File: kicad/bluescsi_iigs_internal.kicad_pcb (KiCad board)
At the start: 2 copper layers, 56.6 x 53.3 mm, 24 parts, among them J1 Conn_02x13_Odd_Even, J2 Conn_02x13_Odd_Even, J3 105162-0001, J4 Conn_01x02_Male, SW1 SW_SPDT, U1 YAAJ_BluePill, U2 UC560x, UCC56xx, U3 UC560x, UCC56xx, U4 AMS1117-5.0

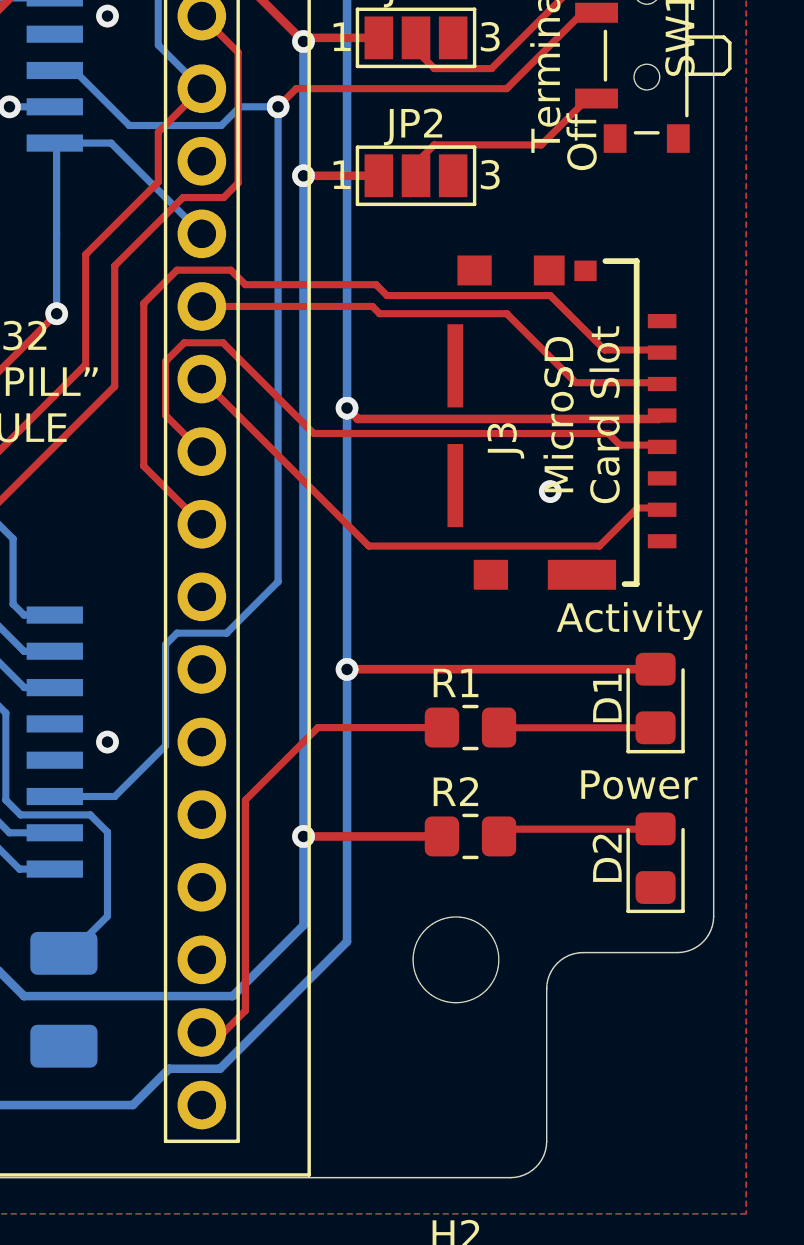
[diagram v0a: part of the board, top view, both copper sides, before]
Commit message: Add p-mosfet driver for activity LED
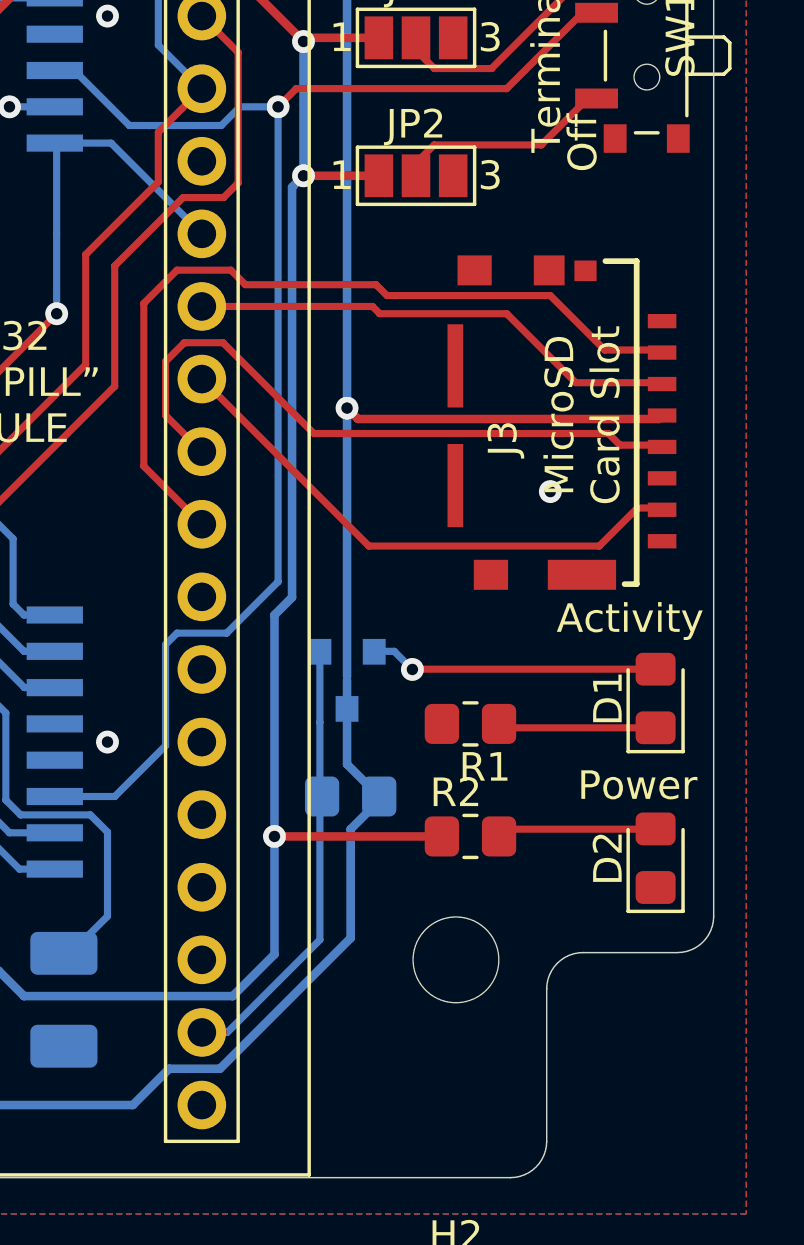
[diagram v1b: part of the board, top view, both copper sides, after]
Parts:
- added Q1: Q_PMOS_GSD, Package_TO_SOT_SMD:SOT-23, B.Cu at (172.7, 84.2)
- added R3: 10K, Resistor_SMD:R_0805_2012Metric_Pad1.20x1.40mm_HandSolder, B.Cu at (172.8, 88.3)
- R1: value 330 -> 470
- R2: value 470 -> 1K
- moved R1 0.13 mm to (177.0, 85.7), turned to 0 degrees
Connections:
- D1 pad 2: +3V3 -> Net-(D1-Pad2)
- R1 pad 1: Net-(D1-Pad1) -> GND
- R1 pad 2: /DISK_ACT -> Net-(D1-Pad1)
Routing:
- net Net-(D1-Pad2): track 0.00 -> 10.1 mm, vias 0 -> 1
- net +3V3: track 85.5 -> 75.7 mm, vias 3 -> 2
- net +5V: track 97.4 -> 98.5 mm
- net /DISK_ACT: track 17.1 -> 16.3 mm

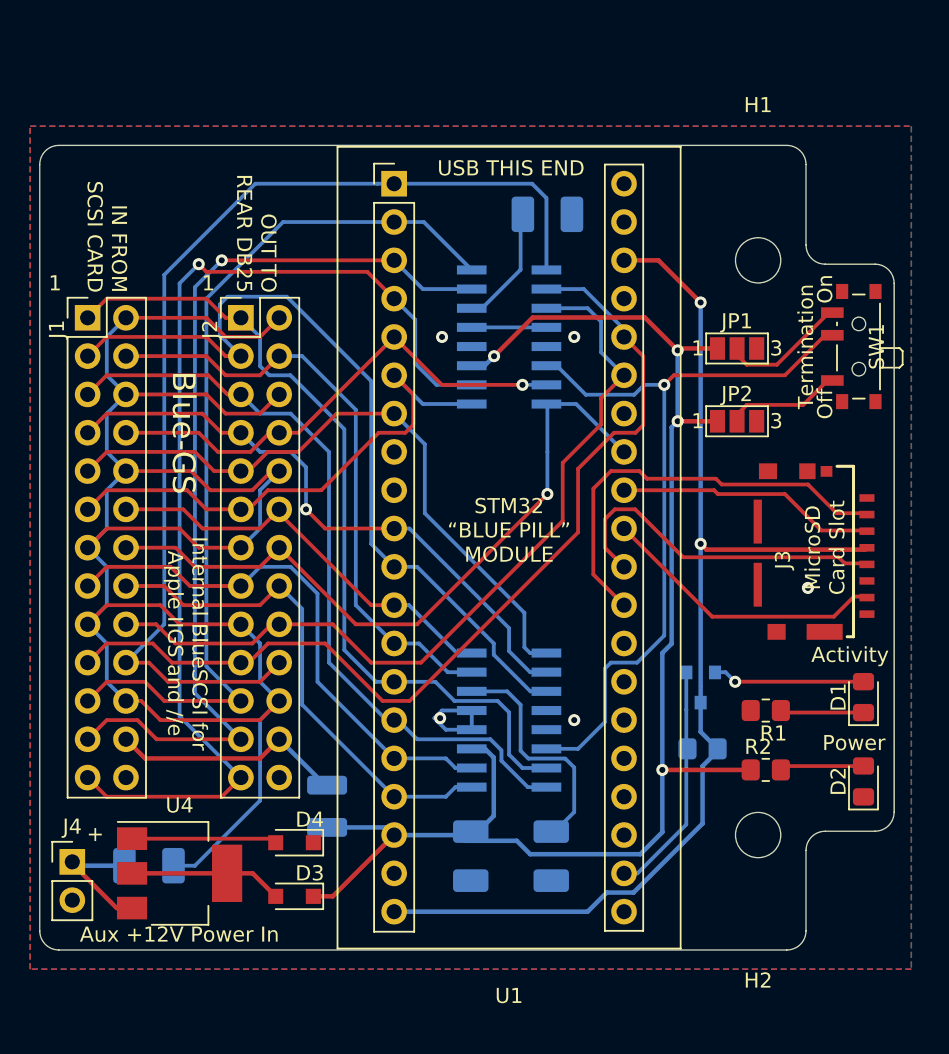
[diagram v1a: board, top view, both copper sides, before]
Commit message: Added connector for external activity LED
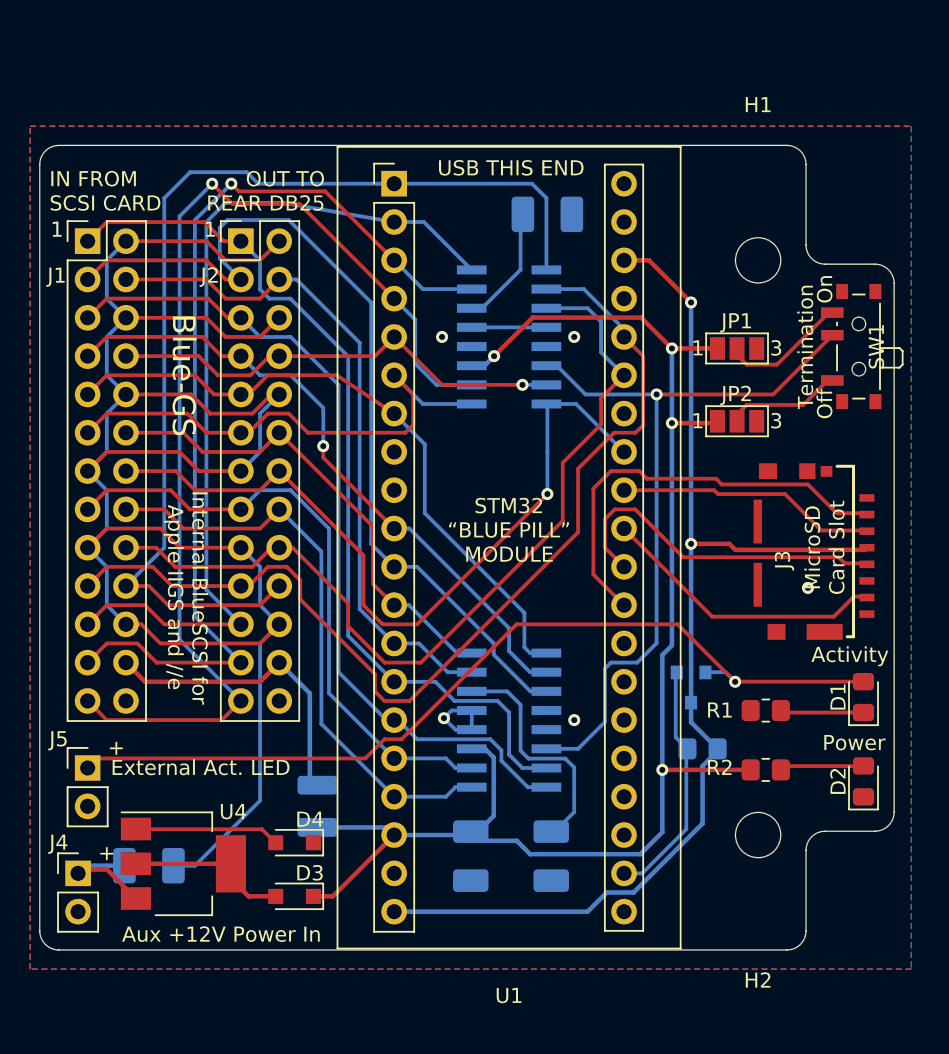
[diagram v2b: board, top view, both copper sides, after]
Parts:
- added J5: Conn_01x02_Male, Connector_PinHeader_2.54mm:PinHeader_1x02_P2.54mm_Vertical, F.Cu at (132.1, 89.5)
- moved J1 5.08 mm to (132.1, 54.6)
- moved J2 5.08 mm to (142.2, 54.6)
- moved J4 0.85 mm to (131.4, 96.5)
- moved U4 0.68 mm to (138.4, 95.9)
- moved F1 0.64 mm to (147.3, 92.1)
- moved Q1 0.63 mm to (172.1, 84.2)
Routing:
- net Net-(D1-Pad2): track 10.1 -> 59.1 mm
- net /SCSI_TERMPWR: track 15.6 -> 21.0 mm
- net /SCSI_MSG: track 54.7 -> 59.8 mm
- net /SCSI_DB1: track 34.2 -> 39.3 mm
- net /SCSI_I_O: track 50.8 -> 55.9 mm
- net /SCSI_DB0: track 36.5 -> 41.6 mm
- net /SCSI_C_D: track 40.2 -> 45.1 mm
- net /SCSI_SEL: track 28.8 -> 33.2 mm
- net /SCSI_REQ: track 55.2 -> 59.6 mm
- net /SCSI_DBP: track 47.1 -> 51.2 mm
- net GND: track 136.7 -> 140.5 mm
- net /SCSI_DB3: track 63.2 -> 66.7 mm
- net /SCSI_DB2: track 54.5 -> 57.5 mm
- net /SCSI_RST: track 40.6 -> 43.0 mm
- net /SCSI_ATN: track 33.4 -> 31.3 mm
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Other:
- board text added: "External Act. LED"
- board text added: "WARNING: USB should not be used while powered from SCSI TermPwr or Aux +12V"
- board text removed: "WARNING: USB should not be used while powered from SCSI Termination Power or Aux +12V Power"

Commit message: Replace mounting holes with Keystone 7774 brackets
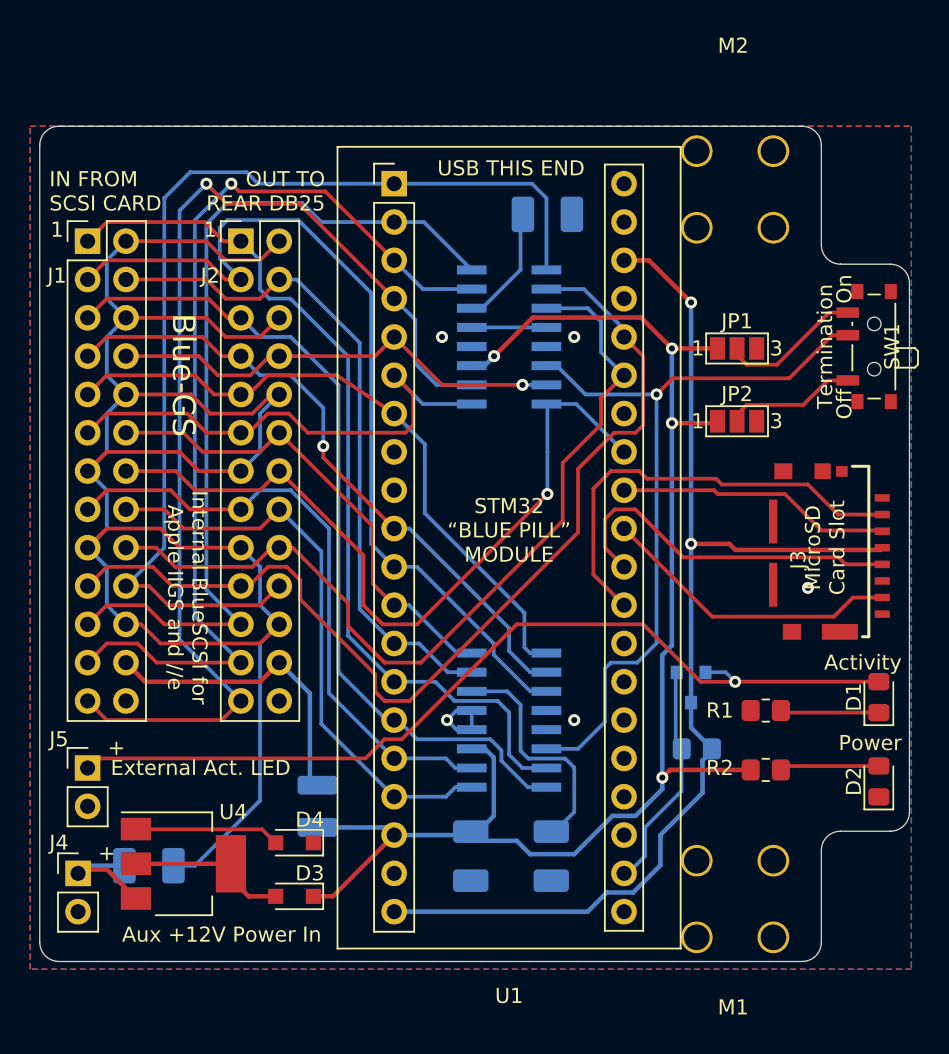
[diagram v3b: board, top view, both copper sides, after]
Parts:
- removed H1, H2: MountingHole, MountingHole:MountingHole_3mm
- added M1: Screw_Terminal_01x01, my library:keystone-7774, F.Cu at (180.7, 100.8)
- added M2: Screw_Terminal_01x01, my library:keystone-7774, F.Cu at (180.7, 53.7)
- moved D1 1.02 mm to (184.5, 84.8)
- moved D2 1.02 mm to (184.5, 90.4)
- moved J3 1.02 mm to (177.4, 75.2)
- moved SW1 1.02 mm to (183.9, 61.6)
- moved R3 0.38 mm to (172.5, 88.3)
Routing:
- net /DISK_ACT: track 16.7 -> 15.1 mm
- net +5V: track 98.8 -> 97.3 mm
- net /TERM_DISC: track 50.1 -> 51.4 mm
- net /TERM_DIS: track 7.57 -> 8.84 mm
- net /TERM_EN: track 8.57 -> 9.84 mm
- net /SD_CSK: track 22.8 -> 23.9 mm
- net /SD_CS: track 28.4 -> 29.4 mm
- net Net-(D1-Pad2): track 59.1 -> 60.1 mm
- net Net-(D1-Pad1): track 5.55 -> 6.56 mm
- net /SD_MOSI: track 17.2 -> 18.2 mm
- net /SD_MISO: track 19.1 -> 20.1 mm
- net +3V3: track 76.0 -> 76.7 mm
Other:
- board size 56.6 x 53.3 mm -> 57.7 x 55.4 mm

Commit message: Adjust screw hole in slightly to account for screw width add silkscreen on rear for card slot
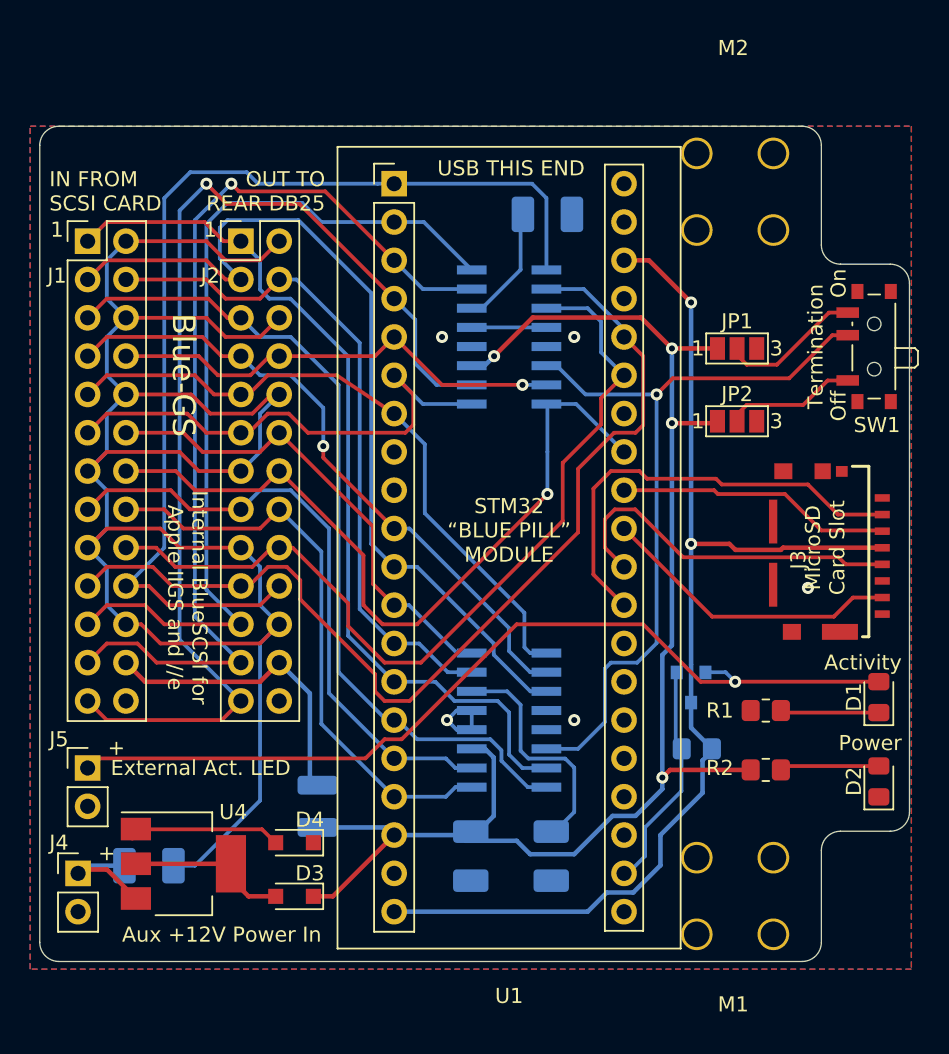
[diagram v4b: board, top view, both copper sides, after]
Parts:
- moved M1 0.20 mm to (180.7, 100.6)
- moved M2 0.15 mm to (180.7, 53.9)
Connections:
- M1 pad 1: (no net) -> GND
- M2 pad 1: (no net) -> GND
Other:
- board text added: "For Apple Rev. C SCSI and cards with compatible connector"
- board text added: "PWR"
- board text added: "WARNING: USB power should not be used while powered from SCSI or Aux +12V"
- board text added: "| CARD |"
- board text removed: "For Apple Rev. C SCSI card, and cards with compatible connector"
- board text removed: "POWER"
- board text removed: "WARNING: USB should not be used while powered from SCSI TermPwr or Aux +12V"

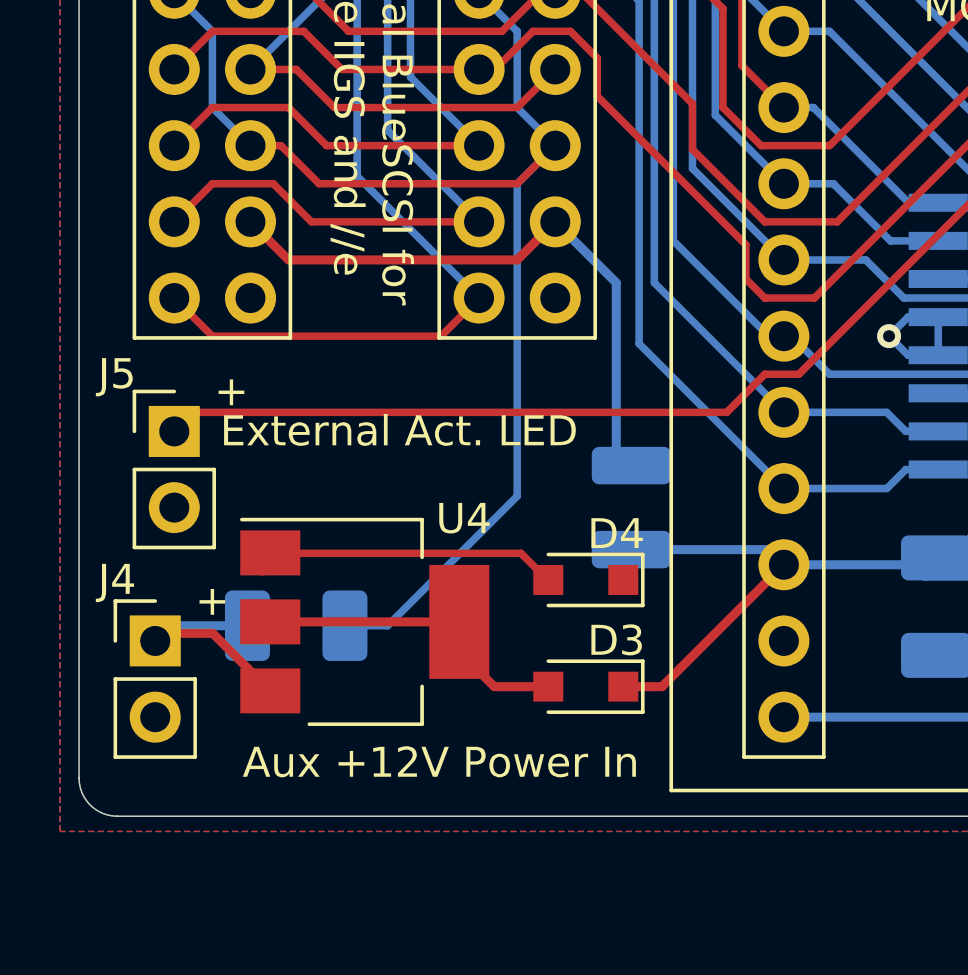
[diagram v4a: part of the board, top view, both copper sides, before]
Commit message: pth regulator hanging off the side
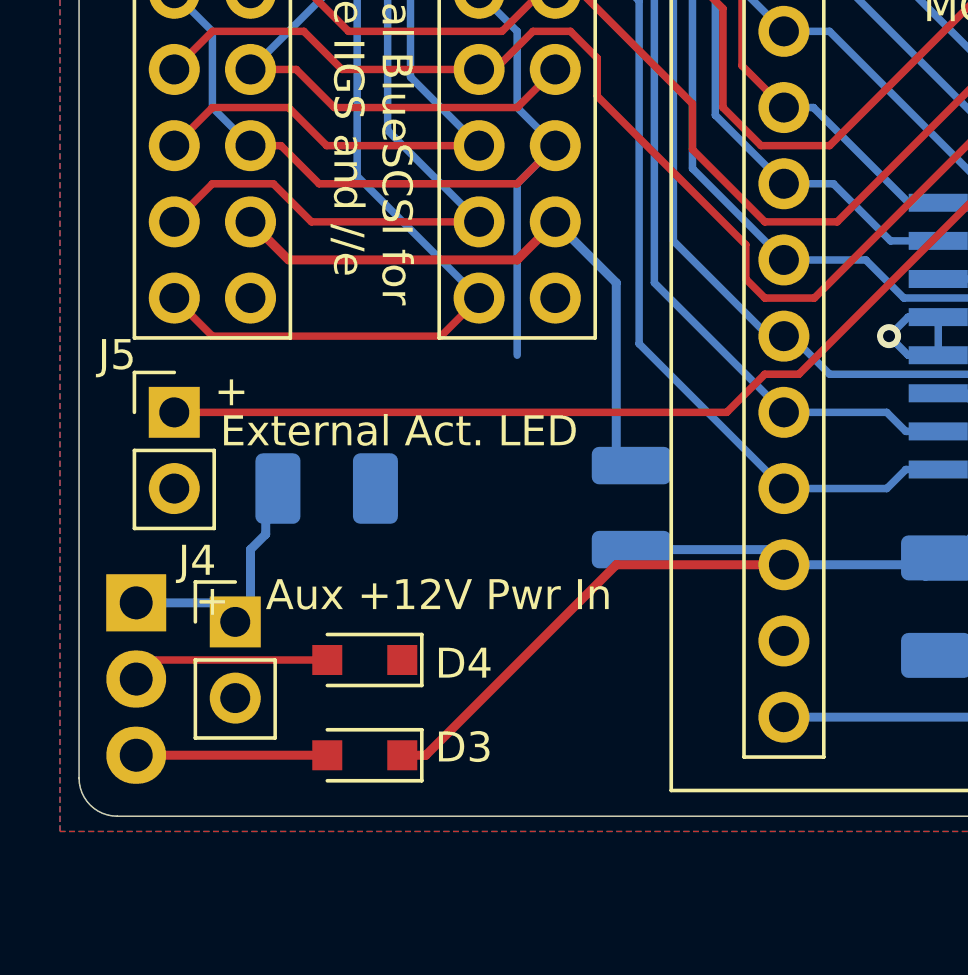
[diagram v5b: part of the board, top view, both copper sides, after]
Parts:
- D3: value 1N5817,1N5817,CUS08F30-H3F -> 1N4001
- D4: value 1N5817,CUS08F30-H3F -> 1N4001
- U4: value AMS1117-5.0 -> MC7805CT-BP; footprint Package_TO_SOT_SMD:SOT-223-3_TabPin2 -> Package_TO_SOT_THT:TO-220-3_Vertical; moved to B.Cu
- moved D4 7.83 mm to (138.4, 97.2)
- moved D3 7.71 mm to (138.4, 100.3)
- moved U4 7.65 mm to (130.8, 95.2), turned to 270 degrees
- moved C4 4.68 mm to (137.2, 91.4)
- moved J4 2.74 mm to (134.1, 95.9)
- moved J5 0.63 mm to (132.1, 88.9)
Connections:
- U4 pad 1: Net-(D4-Pad2) -> /+12V_AUX
- U4 pad 2: /REG_OUT -> Net-(D4-Pad2)
- U4 pad 3: /+12V_AUX -> /REG_OUT
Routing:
- net GND: track 140.1 -> 127.9 mm
- net +5V: track 97.3 -> 105.6 mm
- net /REG_OUT: track 11.8 -> 6.37 mm
- net Net-(D4-Pad2): track 10.2 -> 6.63 mm
- net /+12V_AUX: track 9.03 -> 8.26 mm
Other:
- board text added: "Aux +12V Pwr In"
- board text added: "v1.3 (6/2021)"
- board text removed: "Aux +12V Power In"
- board text removed: "v1.2 (5/2021)"
